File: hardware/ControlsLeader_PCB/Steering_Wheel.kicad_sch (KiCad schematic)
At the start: 20 parts, among them J10 Indicator_Switch, J8 Conn_01x02_Pin, Q2 NMOS, Q5 NMOS, Q6 NMOS, Q9 NMOS

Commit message: Board review
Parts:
- removed C1, C18: 5uF, Capacitor_SMD:C_0805_2012Metric_Pad1.18x1.45mm_HandSolder, symbol Device:C_Small
- removed C16: 5uF, Capacitor_SMD:C_0805_2012Metric, symbol Device:C_Small
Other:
- moved on the sheet: C17, C2, J10, Q2, Q5, R10, R18, R19, R9

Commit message: Schematic Backup
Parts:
- removed C15: 5uF, Capacitor_SMD:C_0805_2012Metric, symbol Device:C_Small
- removed C17, C2: 5uF, Capacitor_SMD:C_0805_2012Metric_Pad1.18x1.45mm_HandSolder, symbol Device:C_Small
- removed Q2, Q5, Q9: NMOS, symbol Simulation_SPICE:NMOS
- removed R10, R18, R19, R9: 100k, Resistor_SMD:R_0805_2012Metric_Pad1.20x1.40mm_HandSolder, symbol Device:R
- removed R21, R8: 100k, symbol Device:R
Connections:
- net +24V: no longer J10.2 (Pin_2)
- net NMOS Switch2/24V_Signal: now reaches J10.1 (Pin_1)
- net NMOS Switch/24V_Signal: now reaches Horn2.2
- net NMOS Switch1/24V_Signal: now reaches J10.3 (Pin_3)
- new net 24V_PWR: J10.2 (Pin_2)
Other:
- added sheet NMOS Switch (NMOS_SW.kicad_sch)
- added sheet NMOS Switch1 (NMOS_SW.kicad_sch)
- added sheet NMOS Switch2 (NMOS_SW.kicad_sch)
- moved on the sheet: Horn2, J10

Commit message: DONE!!! - just need to add footprints + part #s)
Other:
- note added: "Horn 24v -> GPIO -> 24V Signal OUT"
- note added: "Indicator Switches"
- moved on the sheet: Horn2, J10, Q6, R11

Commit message: Schematic Ready for Review - Just need FET footprints to be confirmed
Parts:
- removed J8: Conn_01x02_Pin, symbol Connector:Conn_01x02_Pin
- R11: footprint (none) -> Capacitor_SMD:C_0201_0603Metric_Pad0.64x0.40mm_HandSolder
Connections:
- net 24V_PWR is gone; now on net 3.3V_LDO: J10.2 (Pin_2)
- net +24V renamed 3.3V_LDO
- net NMOS Switch/24V_Signal renamed NMOS Switch3/3.3V_LDO
- net NMOS Switch1/24V_Signal renamed NMOS Switch1/3.3V_LDO
- net NMOS Switch2/24V_Signal renamed NMOS Switch2/3.3V_LDO
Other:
- removed sheet NMOS Switch
- added sheet NMOS Switch3 (NMOS_SW.kicad_sch)
- sheet NMOS Switch1 ports: added 3.3V_LDO, 3.3V_LSOM; removed 24V_Signal, 3.3V_IN
- sheet NMOS Switch2 ports: added 3.3V_LDO, 3.3V_LSOM; removed 24V_Signal, 3.3V_IN

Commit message: Ready for final review
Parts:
- added Regen_Active1: SW_Push, Connector_Molex:Molex_Nano-Fit_105313-xx02_1x02_P2.50mm_Horizontal, symbol Switch:SW_Push
- Horn2: Distributor Link (none) -> https://www.amazon.com/Gebildet-Waterproof-Momentary-Lockle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; Manufacturer (none) -> Amazon
- J10: footprint Connector_Molex:Molex_Micro-Fit_3.0_43650-0300_1x03_P3.00mm_Horizontal -> Connector_Molex:Molex_Nano-Fit_105313-xx03_1x03_P2.50mm_Horizontal; Distributor Link (none) -> https://www.amazon.com/XINYIELE-Rocker-Switch-Position-Circ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; Manufacturer (none) -> Amazon
- Q6: footprint (none) -> LSOM_IRLM:SOT23
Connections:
- net 3.3V_LDO: now also Regen_Active1.1
- new net NMOS Switch8/3.3V_LDO: Regen_Active1.2
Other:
- added sheet NMOS Switch8 (NMOS_SW.kicad_sch)
- moved on the sheet: Horn2, J10, Q6, R11

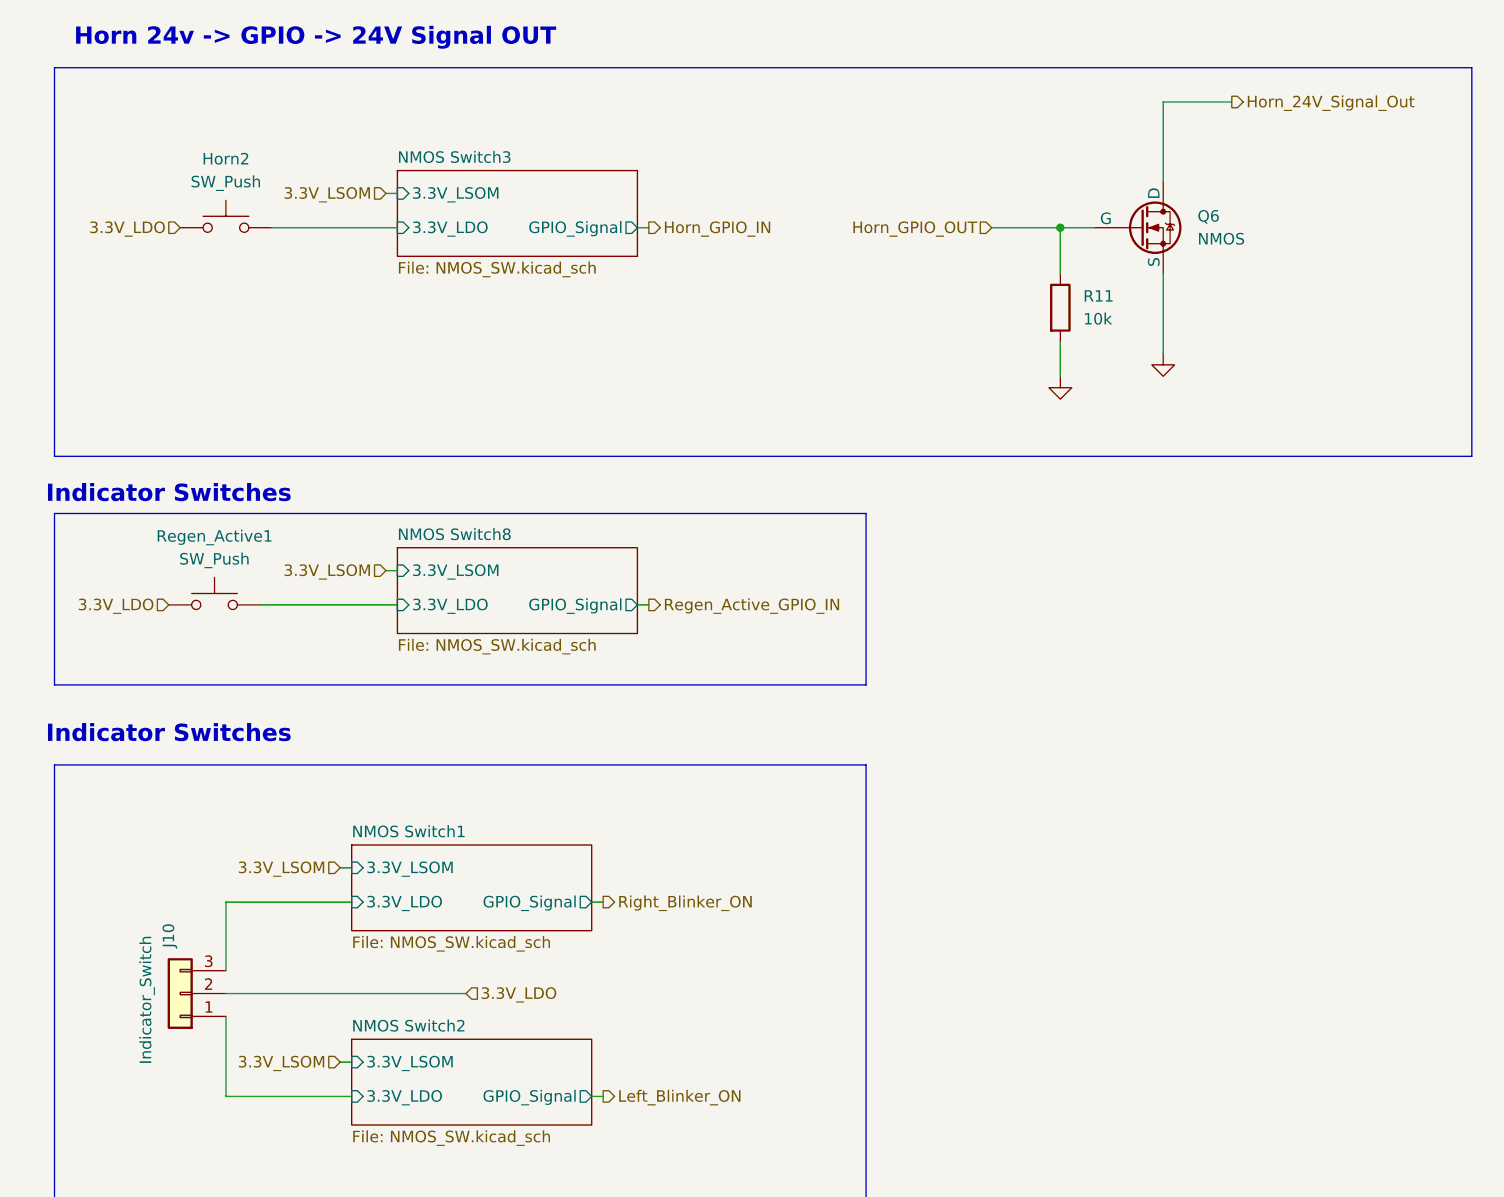
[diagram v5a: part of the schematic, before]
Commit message: Updated LSOM status LED and horn 24v signal connector layout
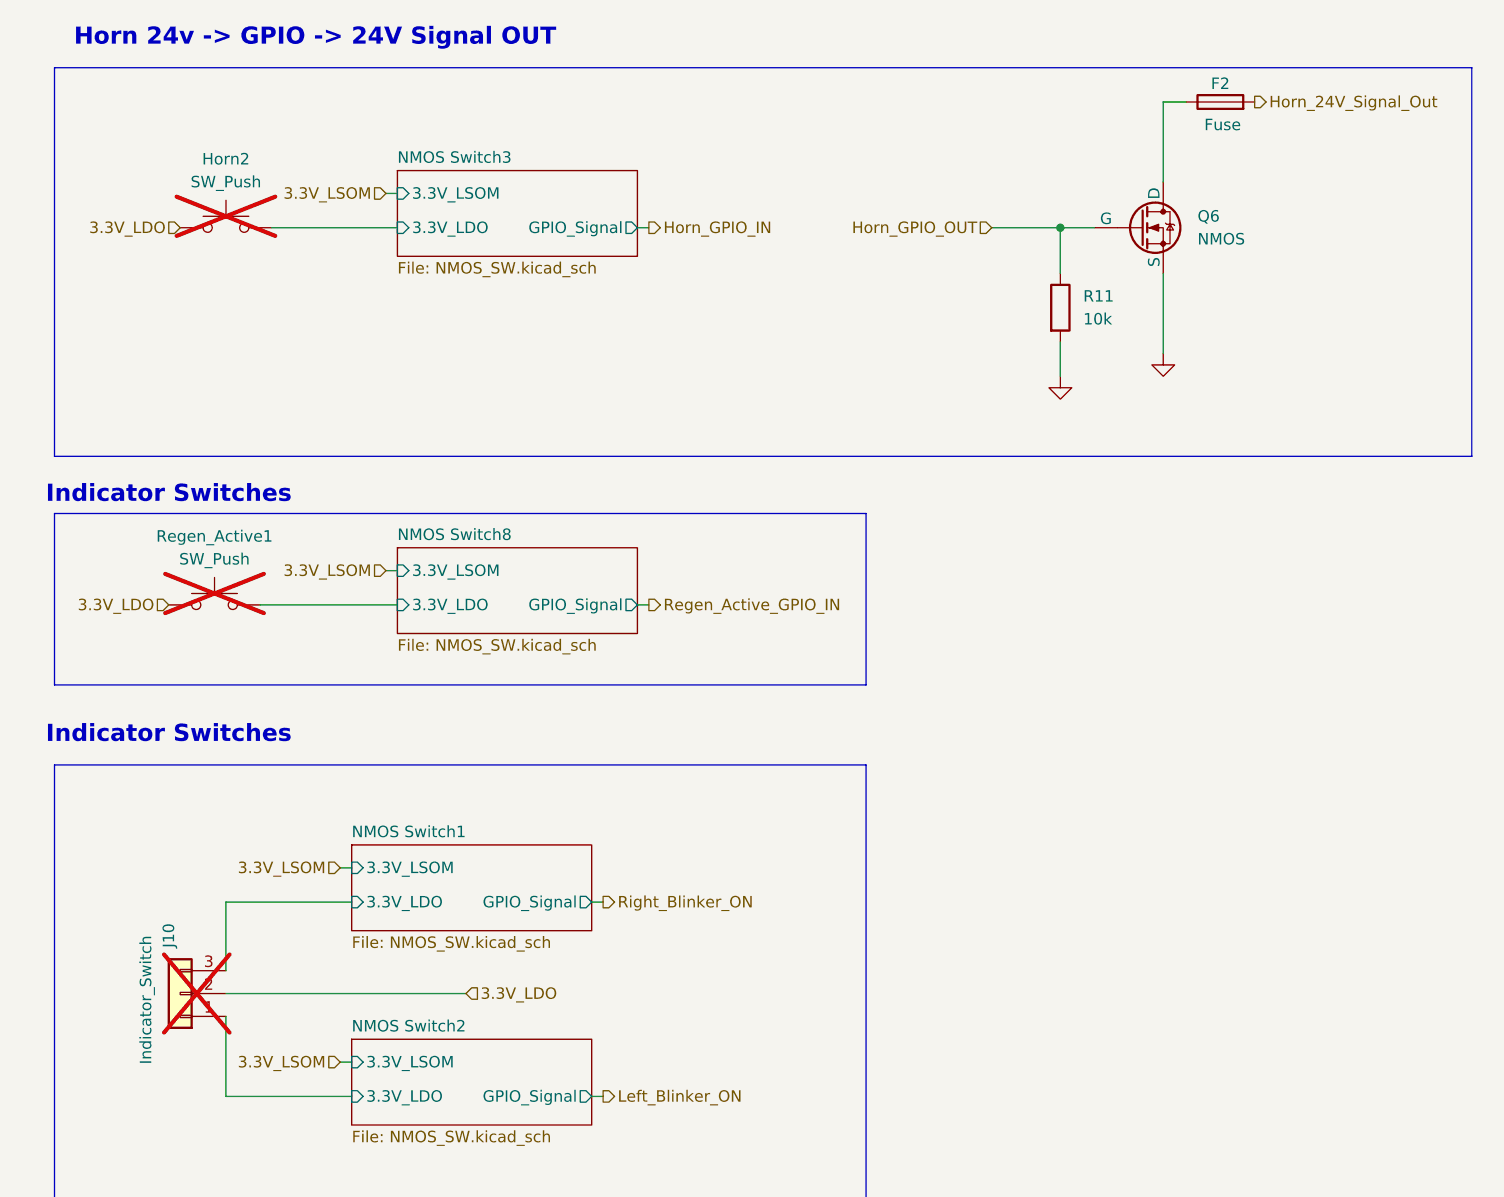
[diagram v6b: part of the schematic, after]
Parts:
- added F2: Fuse, Fuse:Fuseholder_Blade_Mini_Keystone_3568, symbol Device:Fuse
- Horn2, J10, Regen_Active1: now not fitted
- R11: footprint Capacitor_SMD:C_0201_0603Metric_Pad0.64x0.40mm_HandSolder -> Capacitor_SMD:C_0603_1608Metric_Pad1.08x0.95mm_HandSolder
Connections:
- net Horn_24V_Signal_Out: now also F2.2; no longer Q6.1 (D)
- new net: F2.1, Q6.1 (D)
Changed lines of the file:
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@@
+	(wire
+		(pts
+			(xy 189.23 44.45) (xy 191.77 44.45)
+		)
+		(stroke
+			(width 0)
+			(type default)
+		)
+	)
 	(wire
 		(pts
@@
 		(pts
 			(xy 97.79 129.54) (xy 99.06 129.54)
-		)
-		(stroke
-			(width 0)
-			(type default)
-		)
-	)
-	(wire
-		(pts
-			(xy 189.23 44.45) (xy 196.85 44.45)
 		)
 		(stroke
@@
 	(hierarchical_label "Horn_24V_Signal_Out"
 		(shape output)
-		(at 196.85 44.45 0)
+		(at 199.39 44.45 0)
 		(effects
 			(font
@@
 			)
 		)
-		(property "Footprint" "Capacitor_SMD:C_0201_0603Metric_Pad0.64x0.40mm_HandSolder"
+		(property "Footprint" "Capacitor_SMD:C_0603_1608Metric_Pad1.08x0.95mm_HandSolder"
 			(at 176.022 67.31 90)
 			(effects
@@
 		(exclude_from_sim no)
 		(in_bom yes)
-		(on_board yes)
-		(dnp no)
+		(on_board no)
+		(dnp yes)
 		(property "Reference" "J10"
 			(at 78.7399 138.43 90)
@@
 	)
 	(symbol
+		(lib_id "Device:Fuse")
+		(at 195.58 44.45 90)
+		(unit 1)
+		(exclude_from_sim no)
+		(in_bom yes)
+		(on_board yes)
+		(dnp no)
+		(property "Reference" "F2"
+			(at 195.58 42.418 90)
+			(effects
+				(font
+					(size 1.27 1.27)
+				)
+			)
+		)
+		(property "Value" "Fuse"
+			(at 195.834 46.99 90)
+			(effects
+				(font
+					(size 1.27 1.27)
+				)
+			)
+		)
+		(property "Footprint" "Fuse:Fuseholder_Blade_Mini_Keystone_3568"
+			(at 195.58 46.228 90)
+			(effects
+				(font
+					(size 1.27 1.27)
+				)
+				(hide yes)
+			)
+		)
+		(property "Datasheet" "~"
+			(at 195.58 44.45 0)
+			(effects
+				(font
+					(size 1.27 1.27)
+				)
+				(hide yes)
+			)
+		)
+		(property "Description" "Fuse"
+			(at 195.58 44.45 0)
+			(effects
+				(font
+					(size 1.27 1.27)
+				)
+				(hide yes)
+			)
+		)
+		(pin "2"
+		)
+		(pin "1"
+		)
+		(instances
+			(project "ControlsLeader_PCB"
+				(path "/298dad81-302c-41c7-874b-fcde1c3cde17/cf34858a-7a31-4837-b51d-ee9ae3dd074c"
+					(reference "F2")
+					(unit 1)
+				)
+			)
+		)
+	)
+	(symbol
 		(lib_id "Switch:SW_Push")
 		(at 83.82 100.33 0)
@@
 		(exclude_from_sim no)
 		(in_bom yes)
-		(on_board yes)
-		(dnp no)
+		(on_board no)
+		(dnp yes)
 		(fields_autoplaced yes)
 		(property "Reference" "Regen_Active1"
@@
 		(exclude_from_sim no)
 		(in_bom yes)
-		(on_board yes)
-		(dnp no)
+		(on_board no)
+		(dnp yes)
 		(fields_autoplaced yes)
 		(property "Reference" "Horn2"

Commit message: Schematic RevA
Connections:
- net NMOS Switch1/3.3V_LDO renamed NMOS Switch1/3.3V_LDO_Switch
- net NMOS Switch2/3.3V_LDO renamed NMOS Switch2/3.3V_LDO_Switch
- net NMOS Switch3/3.3V_LDO renamed NMOS Switch3/3.3V_LDO_Switch
- net NMOS Switch8/3.3V_LDO renamed NMOS Switch8/3.3V_LDO_Switch
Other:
- sheet NMOS Switch1 ports: added 3.3V_LDO_Switch; removed 3.3V_LDO
- sheet NMOS Switch2 ports: added 3.3V_LDO_Switch; removed 3.3V_LDO
- sheet NMOS Switch3 ports: added 3.3V_LDO_Switch; removed 3.3V_LDO
- sheet NMOS Switch8 ports: added 3.3V_LDO_Switch; removed 3.3V_LDO
- note added: "Change horn label"
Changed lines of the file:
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@@
+		)
+	)
+	(text "Change horn label\n"
+		(exclude_from_sim no)
+		(at 115.062 69.85 0)
+		(effects
+			(font
+				(size 1.27 1.27)
+			)
 		)
 	)
@@
 	(wire
 		(pts
-			(xy 125.73 133.35) (xy 127 133.35)
+			(xy 125.73 129.54) (xy 127 129.54)
 		)
 		(stroke
@@
 	(wire
 		(pts
-			(xy 125.73 154.94) (xy 127 154.94)
+			(xy 125.73 151.13) (xy 127 151.13)
 		)
 		(stroke
@@
 	(wire
 		(pts
-			(xy 130.81 100.33) (xy 132.08 100.33)
+			(xy 130.81 96.52) (xy 132.08 96.52)
 		)
 		(stroke
@@
 	(wire
 		(pts
-			(xy 130.81 58.42) (xy 132.08 58.42)
+			(xy 130.81 54.61) (xy 132.08 54.61)
 		)
 		(stroke
@@
 	(hierarchical_label "Horn_GPIO_IN"
 		(shape output)
-		(at 132.08 58.42 0)
+		(at 132.08 54.61 0)
 		(effects
 			(font
@@
 	(hierarchical_label "Regen_Active_GPIO_IN"
 		(shape output)
-		(at 132.08 100.33 0)
+		(at 132.08 96.52 0)
 		(effects
 			(font
@@
 	(hierarchical_label "Right_Blinker_ON"
 		(shape output)
-		(at 127 133.35 0)
+		(at 127 129.54 0)
 		(effects
 			(font
@@
 	(hierarchical_label "Left_Blinker_ON"
 		(shape output)
-		(at 127 154.94 0)
+		(at 127 151.13 0)
 		(effects
 			(font
@@
 		)
 		(pin "GPIO_Signal" output
-			(at 125.73 133.35 0)
+			(at 125.73 129.54 0)
 			(effects
 				(font
@@
 			)
 		)
-		(pin "3.3V_LDO" input
+		(pin "3.3V_LDO_Switch" input
 			(at 99.06 133.35 180)
 			(effects
@@
 		)
 		(pin "GPIO_Signal" output
-			(at 130.81 58.42 0)
+			(at 130.81 54.61 0)
 			(effects
 				(font
@@
 			)
 		)
-		(pin "3.3V_LDO" input
+		(pin "3.3V_LDO_Switch" input
 			(at 104.14 58.42 180)
 			(effects
@@
 		)
 		(pin "GPIO_Signal" output
-			(at 125.73 154.94 0)
+			(at 125.73 151.13 0)
 			(effects
 				(font
@@
 			)
 		)
-		(pin "3.3V_LDO" input
+		(pin "3.3V_LDO_Switch" input
 			(at 99.06 154.94 180)
 			(effects
@@
 		)
 		(pin "GPIO_Signal" output
-			(at 130.81 100.33 0)
+			(at 130.81 96.52 0)
 			(effects
 				(font
@@
 			)
 		)
-		(pin "3.3V_LDO" input
+		(pin "3.3V_LDO_Switch" input
 			(at 104.14 100.33 180)
 			(effects
